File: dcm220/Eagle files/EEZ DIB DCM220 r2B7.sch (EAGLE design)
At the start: 243 parts, among them IC1 Si8662AB-B-IS1, IC10 MC33272ADR2G, IC11 LT3763EFE#PBF, IC12 MC33274ADR2G, IC13 LT3763EFE#PBF, IC2 TPS54060DGQ, IC3 Si8641AB-B-IS1, IC4 M24C32-WMN6P, IC5 LP2985-33DBVR, IC6 74HC2G04GW,125, IC7 N.C., IC8 STM32F373C8T6, IC9 TL431B, J1 4907, J2 571-0500, J3 571-0100, J4 571-0500, J5 571-0100, Q1 BSP716NH6327XTSA1, Q10 BSS84, Q2 NTD5867NLT4G, Q3 NTD5867NLT4G, Q4 BSS205NH6327XTSA1, Q5 BSS84, Q6 BSP716NH6327XTSA1, Q7 NTD5867NLT4G, Q8 NTD5867NLT4G, Q9 BSS205NH6327XTSA1, X1 39-30-1020, X2 77317-104-28LF, X3 N.C., X4 DS1024-2*5R0, Y1 LF XTAL026392

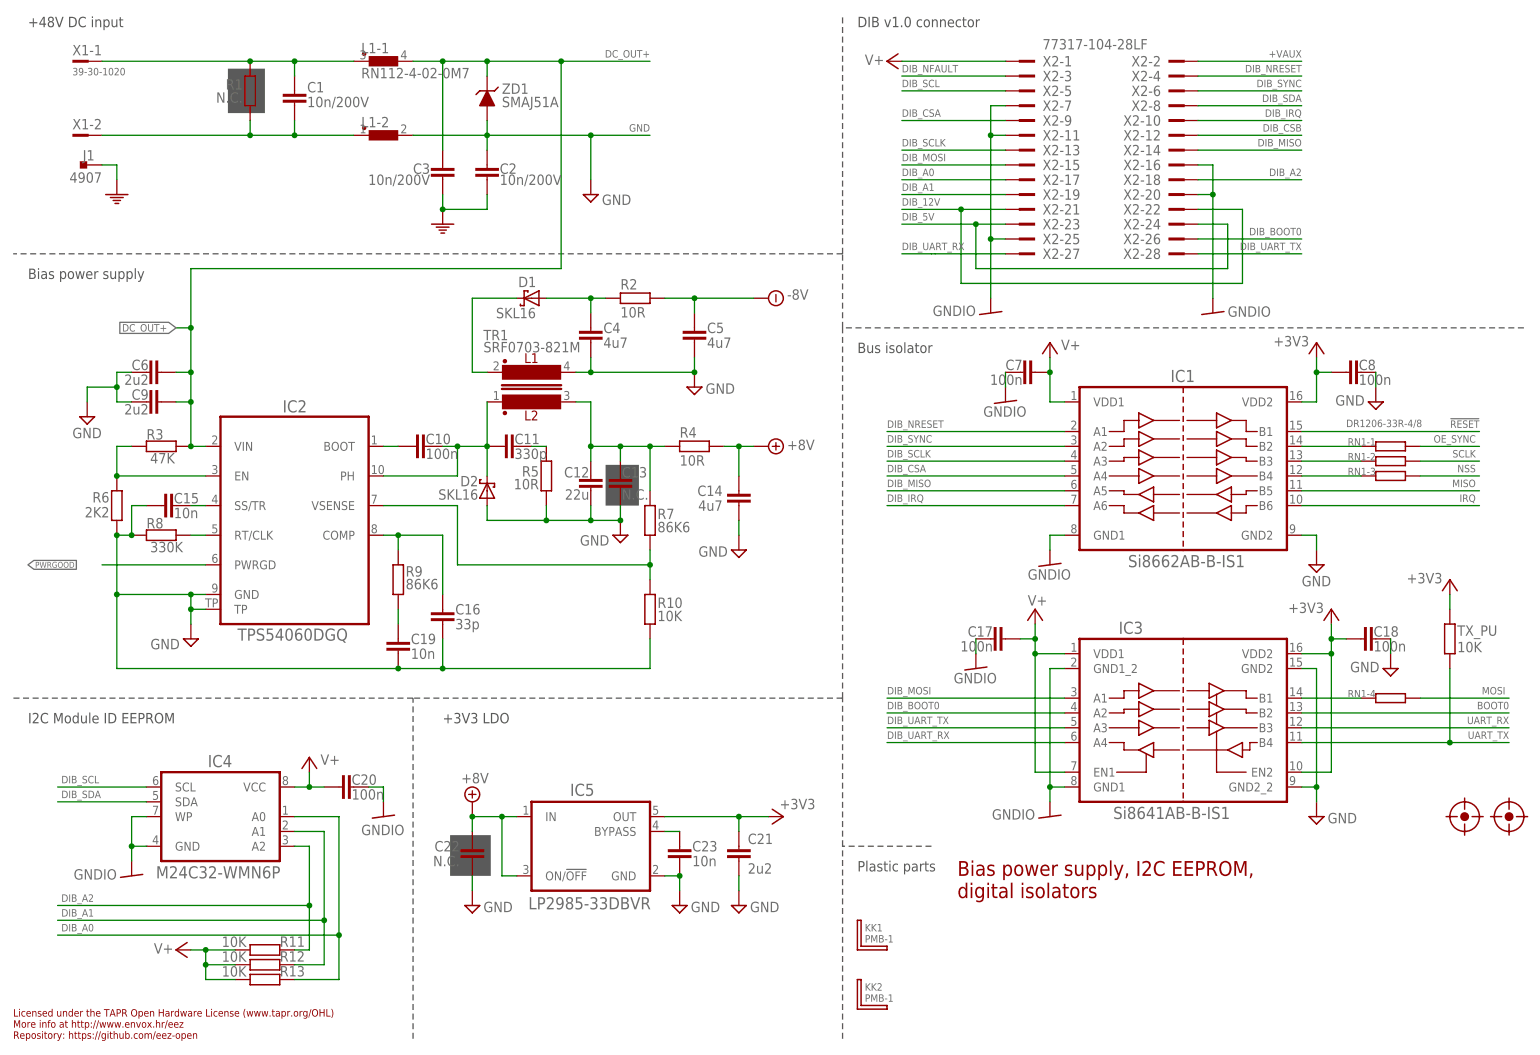
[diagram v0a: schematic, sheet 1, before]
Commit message: DCP405 EEPROM moved, OSHWA UID added
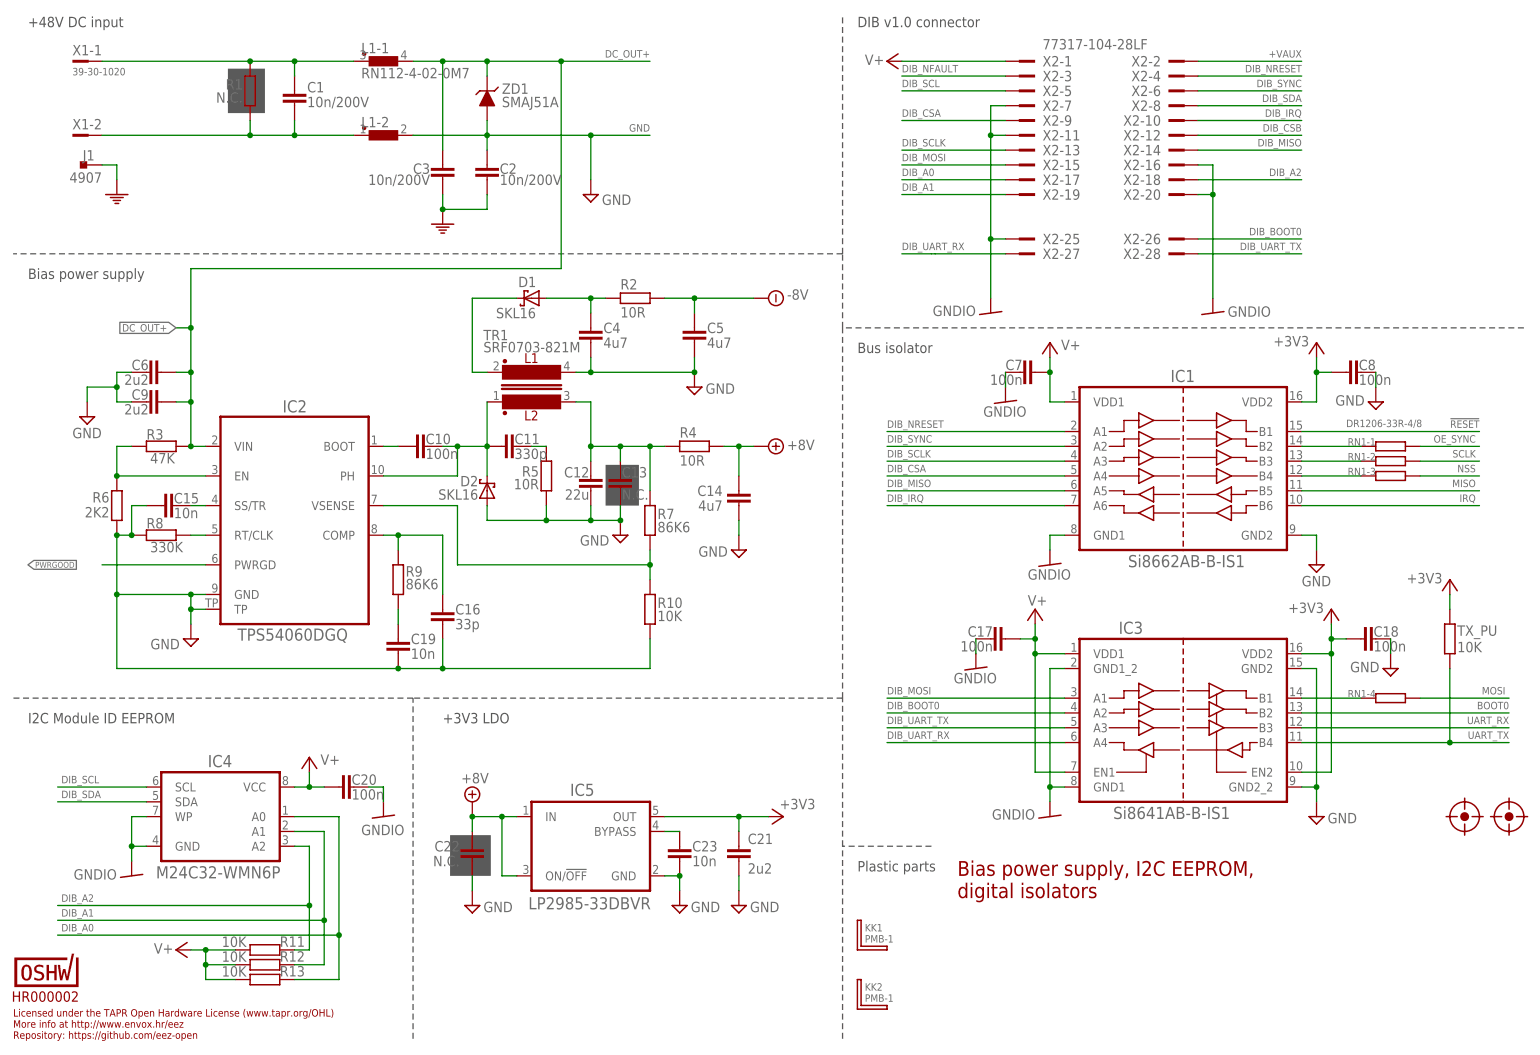
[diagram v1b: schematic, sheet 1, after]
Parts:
- added U$3: HR000002, OSHWA:CERT-SMALL
- R45, R69: value 30K -> 100K
- ZD2, ZD4: value MM3Z2V4T1G -> MM3Z9V1T1G
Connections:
- net N$1 renamed BG1
- net N$15 renamed TG1
- net N$255 renamed TG2
- net N$257 renamed BG2
- removed net DIB_12V: X2-21.1, X2-22.1
- removed net DIB_5V: X2-23.1, X2-24.1
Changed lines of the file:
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@@
 <setting verticaltext="up"/>
 </settings>
-<grid distance="0.1" unitdist="inch" unit="inch" style="lines" multiple="1" display="no" altdistance="0.01" altunitdist="inch" altunit="inch"/>
+<grid distance="0.025" unitdist="inch" unit="inch" style="lines" multiple="4" display="no" altdistance="0.01" altunitdist="inch" altunit="inch"/>
 <layers>
 <layer number="1" name="Top" color="4" fill="1" visible="no" active="no"/>
@@
 <part name="C66" library="rcl" deviceset="C-EU" device="C0805" value="10n"/>
 <part name="C67" library="rcl" deviceset="C-EU" device="C0805" value="4n7"/>
-<part name="R45" library="rcl" deviceset="R-EU_" device="R0805" value="30K"/>
+<part name="R45" library="rcl" deviceset="R-EU_" device="R0805" value="100K"/>
 <part name="SUPPLY10" library="supply2" deviceset="GND" device=""/>
 <part name="C49" library="rcl" deviceset="C-EU" device="C1206" value="4u7"/>
@@
 <part name="C86" library="rcl" deviceset="C-EU" device="C0805" value="10n"/>
 <part name="C87" library="rcl" deviceset="C-EU" device="C0805" value="4n7"/>
-<part name="R69" library="rcl" deviceset="R-EU_" device="R0805" value="30K"/>
+<part name="R69" library="rcl" deviceset="R-EU_" device="R0805" value="100K"/>
 <part name="SUPPLY21" library="supply2" deviceset="GND" device=""/>
 <part name="C70" library="rcl" deviceset="C-EU" device="C1206" value="4u7"/>
@@
 <part name="ZD5" library="EEZ_Lib1" deviceset="P6SMB68A" device="" value="SMAJ51A"/>
 <part name="Q1" library="transistor-power" deviceset="N-HEXFET-2D_?-*" device="SOT232" technology="IRLL014N" value="BSP716NH6327XTSA1"/>
-<part name="ZD2" library="EEZ_Lib1" deviceset="ZENER-DIODE" device="SOD323" value="MM3Z2V4T1G"/>
+<part name="ZD2" library="EEZ_Lib1" deviceset="ZENER-DIODE" device="SOD323" value="MM3Z9V1T1G"/>
 <part name="R28" library="rcl" deviceset="R-EU_" device="R0805" value="10R"/>
 <part name="R29" library="rcl" deviceset="R-EU_" device="R0805" value="86K6"/>
@@
 <part name="R65" library="rcl" deviceset="R-EU_" device="R0805" value="3K3"/>
 <part name="Q6" library="transistor-power" deviceset="N-HEXFET-2D_?-*" device="SOT232" technology="IRLL014N" value="BSP716NH6327XTSA1"/>
-<part name="ZD4" library="EEZ_Lib1" deviceset="ZENER-DIODE" device="SOD323" value="MM3Z2V4T1G"/>
+<part name="ZD4" library="EEZ_Lib1" deviceset="ZENER-DIODE" device="SOD323" value="MM3Z9V1T1G"/>
 <part name="R52" library="rcl" deviceset="R-EU_" device="R0805" value="10R"/>
 <part name="R53" library="rcl" deviceset="R-EU_" device="R0805" value="86K6"/>
@@
 <part name="TX_PU" library="rcl" deviceset="R-EU_" device="R0805" value="10K"/>
 <part name="+3V15" library="supply1" deviceset="+3V3" device=""/>
+<part name="U$3" library="OSHWA" deviceset="CERT" device="-SMALL" value="HR000002"/>
 </parts>
 <sheets>
@@
 <attribute name="NAME" x="199.39" y="148.209" size="1.778" layer="95" rot="R180"/>
 </instance>
-<instance part="X2" gate="-21" x="172.72" y="144.78" smashed="yes" rot="MR0">
-<attribute name="NAME" x="179.07" y="145.669" size="1.778" layer="95" rot="MR180"/>
-</instance>
-<instance part="X2" gate="-22" x="205.74" y="144.78" smashed="yes">
-<attribute name="NAME" x="199.39" y="145.669" size="1.778" layer="95" rot="R180"/>
-</instance>
-<instance part="X2" gate="-23" x="172.72" y="142.24" smashed="yes" rot="MR0">
-<attribute name="NAME" x="179.07" y="143.129" size="1.778" layer="95" rot="MR180"/>
-</instance>
-<instance part="X2" gate="-24" x="205.74" y="142.24" smashed="yes">
-<attribute name="NAME" x="199.39" y="143.129" size="1.778" layer="95" rot="R180"/>
-</instance>
 <instance part="X2" gate="-25" x="172.72" y="139.7" smashed="yes" rot="MR0">
 <attribute name="NAME" x="179.07" y="140.589" size="1.778" layer="95" rot="MR180"/>
@@
 <attribute name="VALUE" x="247.65" y="80.645" size="1.778" layer="96" rot="MR0"/>
 </instance>
+<instance part="U$3" gate="G$1" x="8.255" y="11.43" smashed="yes">
+<attribute name="VALUE" x="2.286" y="8.89" size="1.778" layer="94" font="vector" ratio="12"/>
+</instance>
 </instances>
 <busses>
@@
 </segment>
 </net>
-<net name="DIB_5V" class="0">
-<segment>
-<wire x1="167.64" y1="142.24" x2="172.72" y2="142.24" width="0.1524" layer="91"/>
-<wire x1="167.64" y1="142.24" x2="167.64" y2="134.62" width="0.1524" layer="91"/>
-<wire x1="210.82" y1="142.24" x2="205.74" y2="142.24" width="0.1524" layer="91"/>
-<wire x1="167.64" y1="134.62" x2="210.82" y2="134.62" width="0.1524" layer="91"/>
-<wire x1="210.82" y1="134.62" x2="210.82" y2="142.24" width="0.1524" layer="91"/>
-<wire x1="167.64" y1="142.24" x2="154.94" y2="142.24" width="0.1524" layer="91"/>
-<junction x="167.64" y="142.24"/>
-<label x="154.94" y="142.875" size="1.27" layer="102"/>
-<pinref part="X2" gate="-24" pin="1"/>
-<pinref part="X2" gate="-23" pin="1"/>
-</segment>
-</net>
 <net name="DIB_SCL" class="0">
 <segment>
@@
 </segment>
 </net>
-<net name="DIB_12V" class="0">
-<segment>
-<wire x1="165.1" y1="144.78" x2="172.72" y2="144.78" width="0.1524" layer="91"/>
-<wire x1="165.1" y1="144.78" x2="165.1" y2="132.08" width="0.1524" layer="91"/>
-<wire x1="213.36" y1="144.78" x2="205.74" y2="144.78" width="0.1524" layer="91"/>
-<wire x1="165.1" y1="132.08" x2="213.36" y2="132.08" width="0.1524" layer="91"/>
-<wire x1="213.36" y1="132.08" x2="213.36" y2="144.78" width="0.1524" layer="91"/>
-<wire x1="165.1" y1="144.78" x2="154.94" y2="144.78" width="0.1524" layer="91"/>
-<junction x="165.1" y="144.78"/>
-<label x="154.94" y="145.415" size="1.27" layer="102"/>
-<pinref part="X2" gate="-22" pin="1"/>
-<pinref part="X2" gate="-21" pin="1"/>
-</segment>
-</net>
 <net name="DIB_NFAULT" class="0">
 <segment>
@@
 </segment>
 </net>
-<net name="N$15" class="0">
+<net name="TG1" class="0">
 <segment>
 <pinref part="IC11" gate="G$1" pin="TG"/>
@@
 </segment>
 </net>
-<net name="N$1" class="0">
+<net name="BG1" class="0">
 <segment>
 <pinref part="IC11" gate="G$1" pin="BG"/>
@@
 </segment>
 </net>
-<net name="N$255" class="0">
+<net name="TG2" class="0">
 <segment>
 <pinref part="IC13" gate="G$1" pin="TG"/>
@@
 </segment>
 </net>
-<net name="N$257" class="0">
+<net name="BG2" class="0">
 <segment>
 <pinref part="IC13" gate="G$1" pin="BG"/>

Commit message: #64
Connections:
- net DIB_BOOT0: now also IC3.EN1
- net V+: no longer IC3.EN1
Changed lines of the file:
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@@
 </segment>
 <segment>
-<pinref part="IC3" gate="A" pin="EN1"/>
-<wire x1="182.88" y1="48.26" x2="177.8" y2="48.26" width="0.1524" layer="91"/>
-<wire x1="177.8" y1="48.26" x2="177.8" y2="68.58" width="0.1524" layer="91"/>
 <pinref part="IC3" gate="A" pin="VDD1"/>
 <wire x1="177.8" y1="68.58" x2="182.88" y2="68.58" width="0.1524" layer="91"/>
 <wire x1="177.8" y1="68.58" x2="177.8" y2="71.12" width="0.1524" layer="91"/>
-<junction x="177.8" y="68.58"/>
 <pinref part="SUPPLY39" gate="1" pin="V+"/>
 <pinref part="C17" gate="G$1" pin="1"/>
@@
 <wire x1="182.88" y1="58.42" x2="152.4" y2="58.42" width="0.1524" layer="91"/>
 </segment>
-</net>
+<segment>
+<pinref part="IC3" gate="A" pin="EN1"/>
+<wire x1="182.88" y1="48.26" x2="152.4" y2="48.26" width="0.1524" layer="91"/>
+<label x="152.4" y="48.895" size="1.27" layer="102"/>
+</segment>
+</net>
